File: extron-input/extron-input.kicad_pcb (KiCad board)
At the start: 2 copper layers, 92 x 37 mm, 22 parts, among them J1 SCART-F, J10 Conn_01x01, J11 Conn_01x01, J2 RED, J3 GREEN, J4 BLUE, J5 SYNC, J6 PHOENIX, J7 SENSE, J8 Conn_01x01, J9 Conn_01x01, SW1 SW_DPDT_x2, U1 LM1881

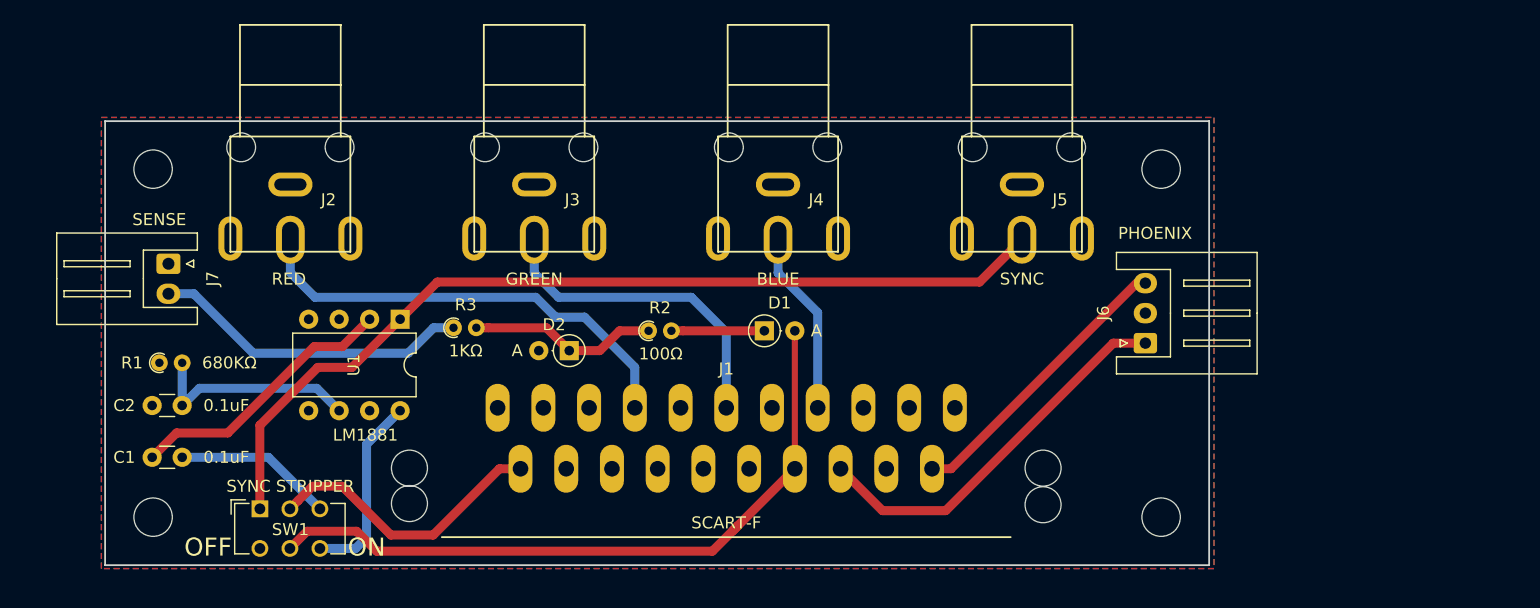
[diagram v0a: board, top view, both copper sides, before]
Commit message: WIP on input board v3
New features:
  Longer boards that support top/bottom placement, allowing closer
  placement for extron 300 ADSP models, and allowing thicker FR4 again

  Will have new RCA placements to support both older and newer extron
  BNC spacings
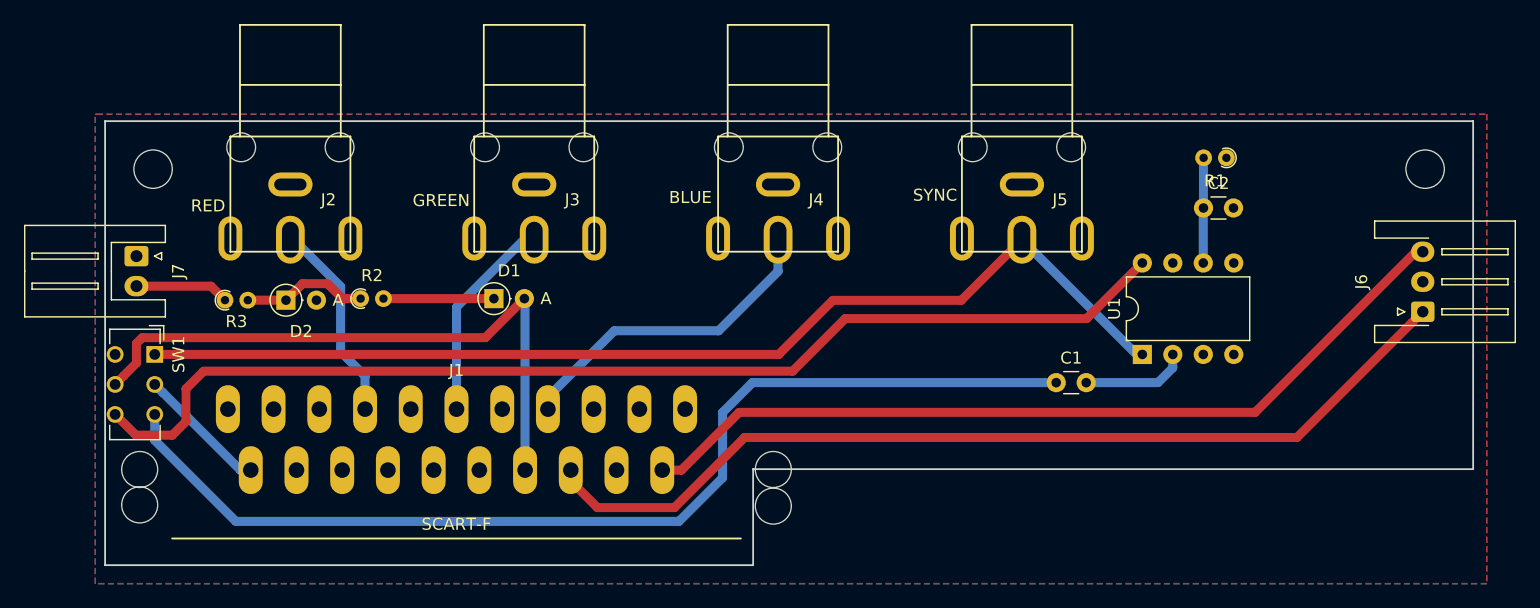
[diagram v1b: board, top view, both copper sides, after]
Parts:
- removed J11, J9: Conn_01x01, MountingHole:MountingHole_3.2mm_M3
- removed REF**: KiCad-Logo_5mm_SilkScreen, Symbol:KiCad-Logo_5mm_SilkScreen
- removed REF**: OSHW-Logo_7.5x8mm_SilkScreen, Symbol:OSHW-Logo_7.5x8mm_SilkScreen
- J6: footprint Connector_JST:JST_XH_S03B-XH-A_1x03_P2.50mm_Horizontal -> Connector_JST:JST_XH_S3B-XH-A-1_1x03_P2.50mm_Horizontal
- J7: footprint Connector_JST:JST_XH_S02B-XH-A_1x02_P2.50mm_Horizontal -> Connector_JST:JST_XH_S2B-XH-A_1x02_P2.50mm_Horizontal
- moved R1 90.5 mm to (169.4, 79.1), turned to 180 degrees
- moved C2 86.7 mm to (167.5, 83.2), turned to 0 degrees
- moved C1 73.1 mm to (155.3, 97.8), turned to 0 degrees
- moved U1 61.9 mm to (162.4, 95.4), turned to 90 degrees
- moved R2 24.1 mm to (97.3, 90.8)
- moved D2 24.0 mm to (91.1, 90.9), turned to 0 degrees
- moved J6 23.3 mm to (185.8, 91.9)
- moved D1 22.7 mm to (108.4, 90.8)
- moved J1 22.5 mm to (105.3, 105.1)
- moved J8 22.0 mm to (186.0, 80.0)
- moved R3 19.2 mm to (86.0, 90.9)
- moved SW1 15.6 mm to (80.1, 95.4), turned to 270 degrees
- moved J7 2.74 mm to (78.6, 87.2)
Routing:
- net Net-(SW1-Pad6): track 16.0 -> 94.2 mm
- net Net-(C1-Pad1): track 13.3 -> 88.0 mm
- net Net-(J1-Pad6): track 32.6 -> 79.6 mm
- net Net-(J1-Pad2): track 24.2 -> 70.9 mm
- net RED: track 38.1 -> 16.9 mm
- net Net-(J7-Pad2): track 26.7 -> 7.86 mm
- net SYNC: track 76.9 -> 91.6 mm
- net Net-(C1-Pad2): track 22.9 -> 8.84 mm
- net Net-(J1-Pad20): track 24.0 -> 11.0 mm
- net BLUE: track 15.4 -> 27.2 mm
- net GREEN: track 27.1 -> 17.3 mm
- net Net-(C2-Pad1): track 18.0 -> 8.79 mm
- net SENSE: track 58.4 -> 52.4 mm
- net Net-(D2-Pad1): track 15.8 -> 10.5 mm
- net Net-(D1-Pad1): track 7.75 -> 9.20 mm
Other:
- board size 92 x 37 mm -> 114 x 37 mm
- board text removed: "LM1881"
- board text removed: "OFF"
- board text removed: "ON"
- board text removed: "SYNC STRIPPER"
